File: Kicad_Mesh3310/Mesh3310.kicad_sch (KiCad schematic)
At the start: 16 parts, among them J1 USB device, SW2 "OK"

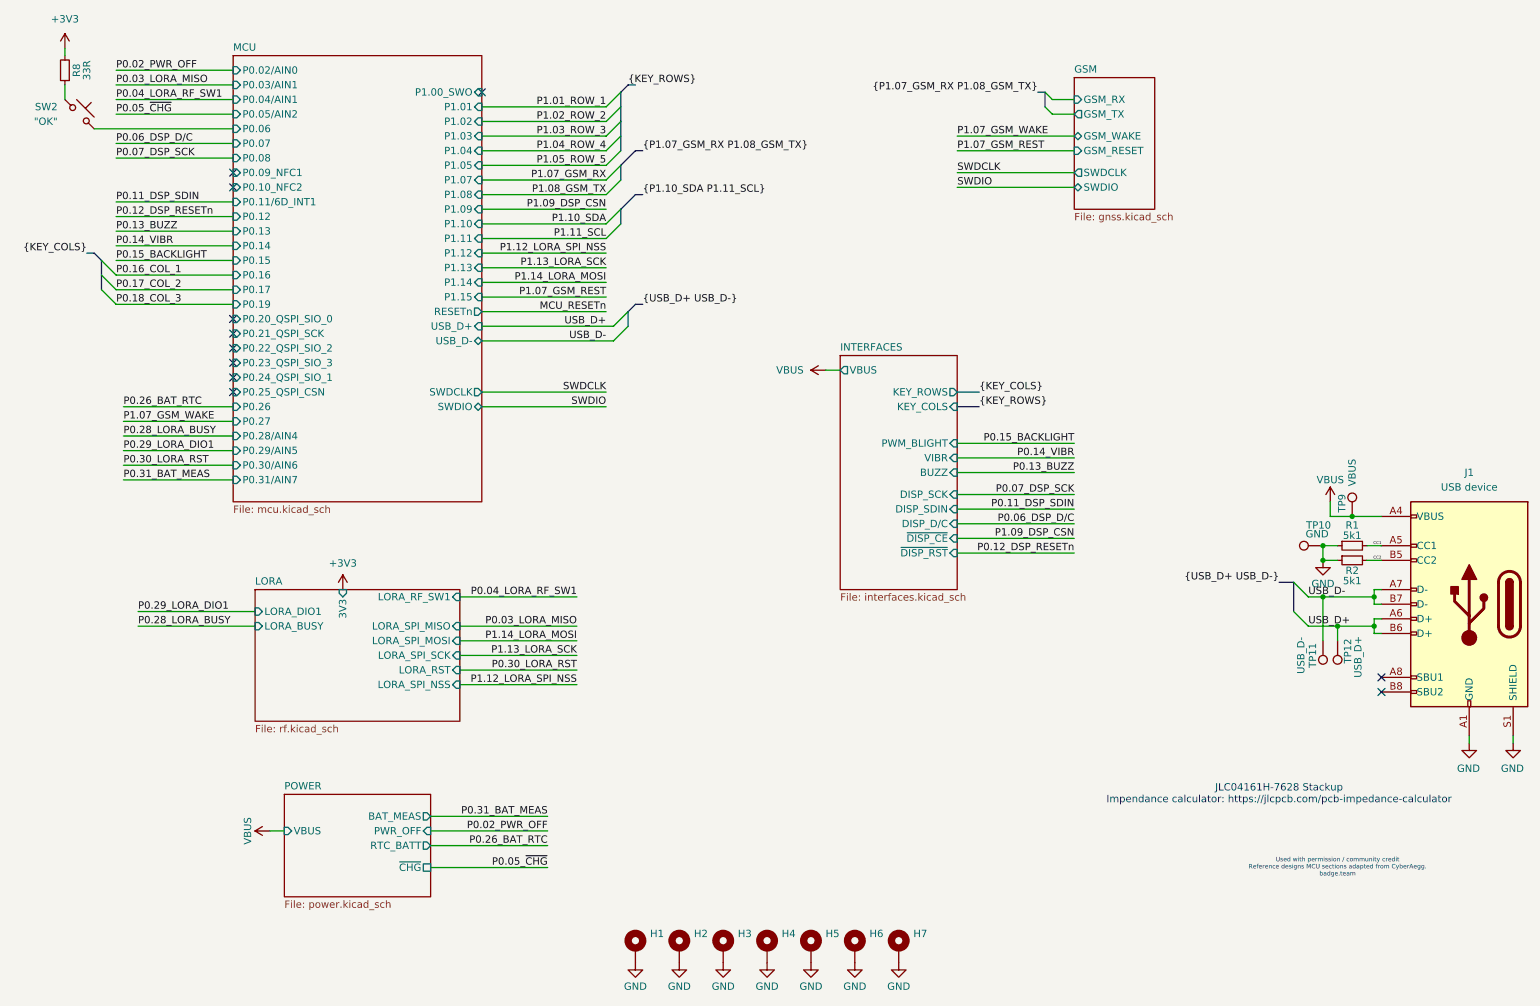
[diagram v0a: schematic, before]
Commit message: Schema afgemaakt, 6-laags layout, LCSC-onderdelen en productiebestanden
- schema opgeschoond en aangevuld (ERC 0)
- bord naar 6 lagen (JLC06161H-3313), volledig gerouteerd, DRC 0
- LTE via U.FL, USB via bodemconnector J4
- LCSC-nummers voor alle onderdelen, datasheets toegevoegd
- gerbers, boorbestanden, positiebestand en stuklijst in productie/
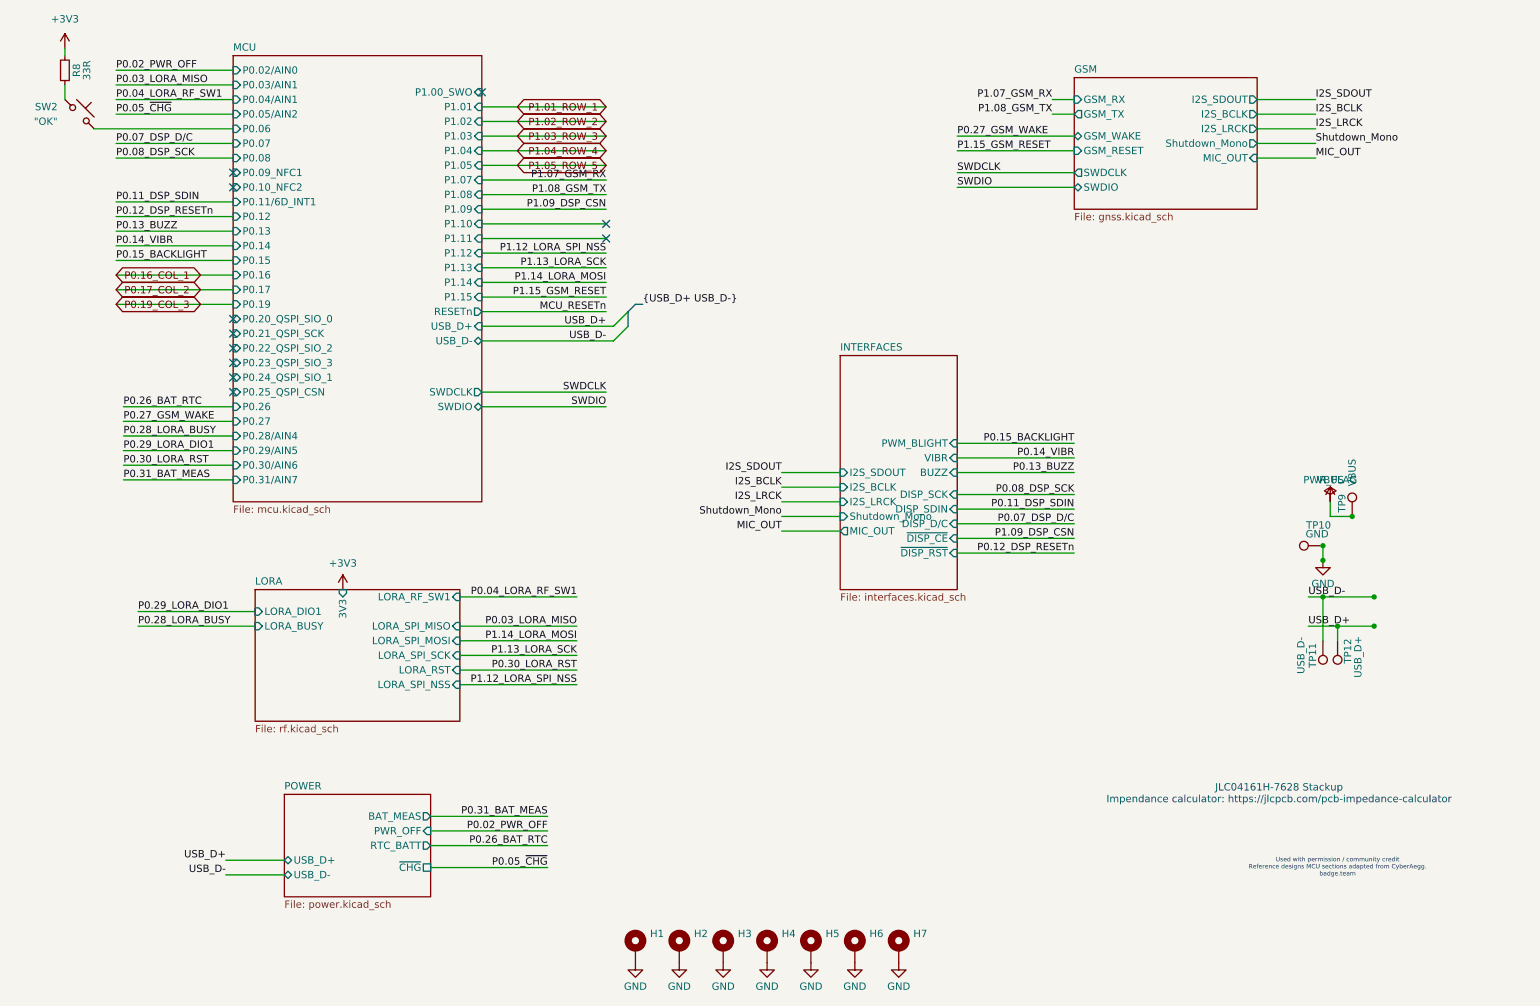
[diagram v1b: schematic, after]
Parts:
- removed J1: USB device, mesh3310_footprints:USB_C_Receptacle_HRO_TYPE-C-31-M-12, symbol Connector:USB_C_Receptacle_USB2.0_16P
- removed R1, R2: 5k1, Resistor_SMD:R_0201_0603Metric, symbol mch2021-rescue:R_Small-Device
- R8: LCSC C25105 -> C423356
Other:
- sheet GSM ports: added I2S_BCLK, I2S_LRCK, I2S_SDOUT, MIC_OUT, Shutdown_Mono; removed none
- sheet INTERFACES ports: added I2S_BCLK, I2S_LRCK, I2S_SDOUT, MIC_OUT, Shutdown_Mono; removed KEY_COLS, KEY_ROWS, VBUS
- sheet POWER ports: added USB_D+, USB_D-; removed VBUS

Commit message: Rev. F + G: controleronde, TPS3420 aan/uit-knop, FLASH_CS pull-up, RF4 DNP, U.FL-variant LoRa
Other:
- sheet POWER ports: added PWR_KNOP; removed RTC_BATT
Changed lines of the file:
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@@
 		(title "Mainboard replacement for Nokia 3310")
 		(date "29-12-2025")
-		(rev "Rev A")
+		(rev "Rev G")
 		(company "Mesh3310")
 		(comment 1 "JDJ electronics")
@@
 		)
 	)
-	(label "P0.26_BAT_RTC"
+	(label "P0.26_PWR_KNOP"
 		(at 33.02 93.98 0)
 		(effects
@@
 		)
 	)
-	(label "P0.26_BAT_RTC"
+	(label "P0.26_PWR_KNOP"
 		(at 106.68 170.18 180)
 		(effects
@@
 			)
 		)
-		(pin "RTC_BATT" output
+		(pin "PWR_KNOP" output
 			(at 86.36 170.18 0)
 			(effects
